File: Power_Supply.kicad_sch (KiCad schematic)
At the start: 23 parts, among them J1 Barrel_Jack, Q25 KSP2907A, Q26 IRF644, SW1 PB400EEQX, U1 L7805, U2 MC34063AP

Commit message: layout started
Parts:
- added C9: 100n, Capacitor_THT:C_Rect_L7.0mm_W2.5mm_P5.00mm, symbol Device:C
- F1: footprint Fuse:Fuseholder_Cylinder-5x20mm_Schurter_0031_8201_Horizontal_Open -> NixieClock:5x20 fuse
- Q25: footprint Package_TO_SOT_THT:TO-92_Inline -> Package_TO_SOT_THT:TO-92_Inline_Wide
- SW1: footprint Button_Switch_THT:SW_NKK_BB15AH -> NixieClock:PB400EEQX
- renumbered C9 to C10, C10 to C11, C11 to C12, C12 to C13, C13 to C14
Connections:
- net +12V: now also C9.1
- net GND: now also C9.2
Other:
- moved on the sheet: C10, C8, U1

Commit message: Layout completed
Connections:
- net SMPS_IN: now reaches L1.1, R51.1, R52.1, U2.1 (SwC), U2.7 (Ipk), U2.8 (DC)
- net SMPS_SW: now reaches D3.2 (A), L1.2, Q26.2 (D)
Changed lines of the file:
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@@
     (effects (font (size 2.0066 2.0066)) (justify left bottom))
+  )
+  (label "SMPS_OUT" (at 241.3 78.74 0)
+    (effects (font (size 1.27 1.27)) (justify left bottom))
+  )
+  (label "SMPS_SW" (at 223.52 77.47 180)
+    (effects (font (size 1.27 1.27)) (justify right bottom))
+  )
+  (label "SMPS_IN" (at 196.85 60.96 0)
+    (effects (font (size 1.27 1.27)) (justify left bottom))
   )
   (global_label "DISP_EN" (shape input) (at 128.27 45.72 180) (fields_autoplaced)

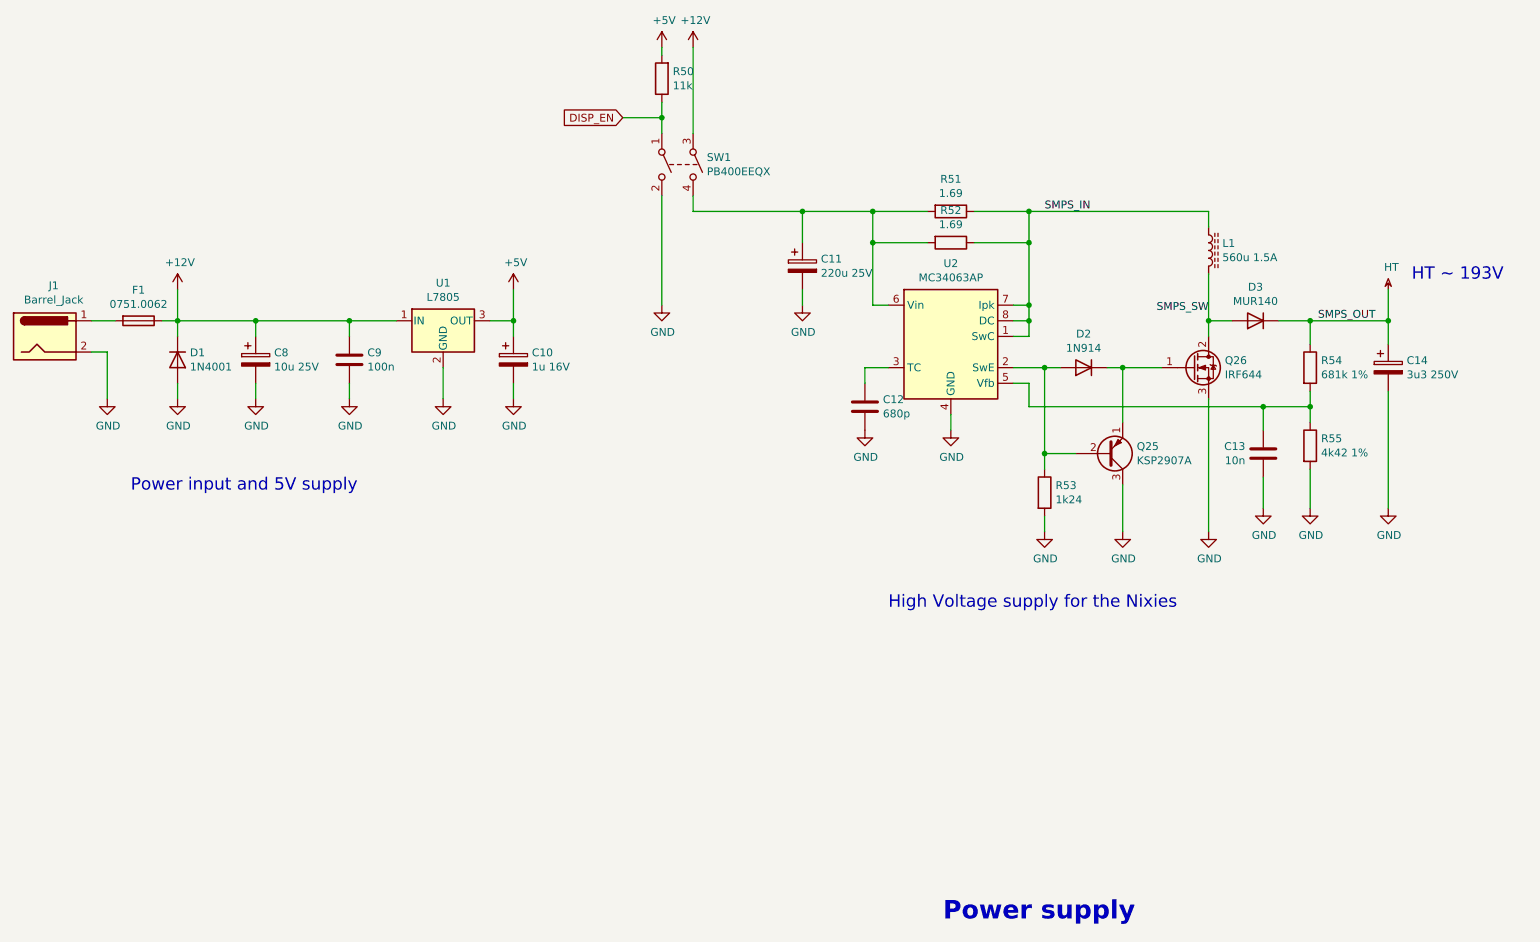
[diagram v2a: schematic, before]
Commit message: Pablo's review, several changes:
Schematic:
- Overall aesthetics
- Added PWR_FLAG to remove ERC errors.
Layout:
- Overall component alignment
- Removed some loops and unnecessary vias.
- Cleaned up vias without ends.
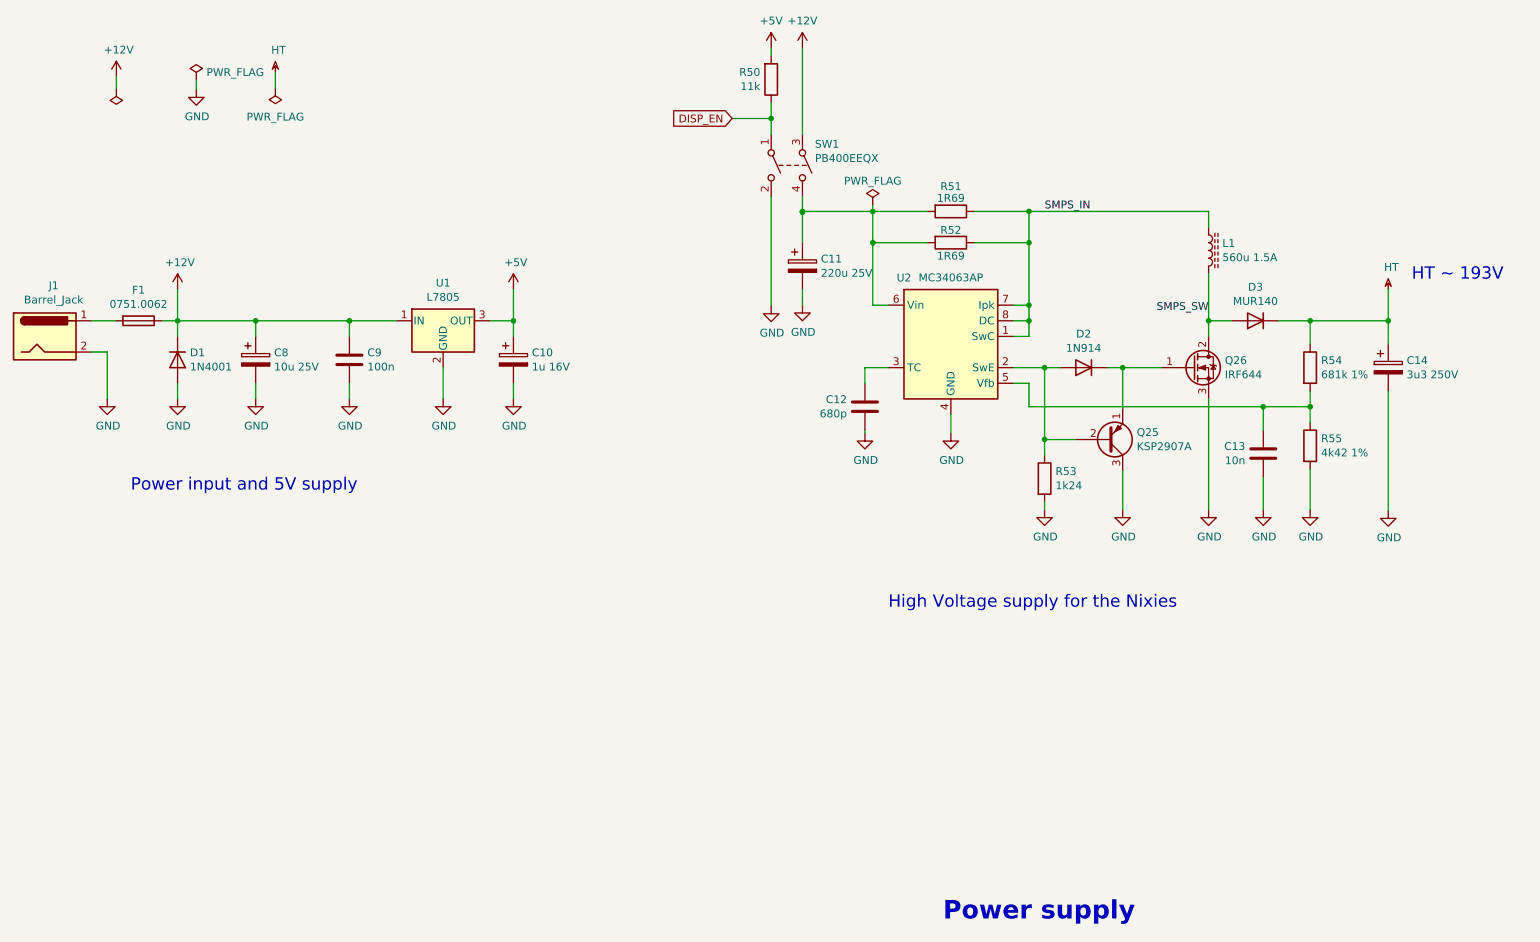
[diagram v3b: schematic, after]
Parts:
- R51, R52: value 1.69 -> 1R69
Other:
- moved on the sheet: Q25, R50, R53, SW1

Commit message: WIP
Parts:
- C13: footprint Capacitor_THT:C_Rect_L7.0mm_W2.5mm_P5.00mm -> Capacitor_SMD:C_0805_2012Metric
- R50, R51, R52, R53, R54, R55: footprint Resistor_THT:R_Axial_DIN0207_L6.3mm_D2.5mm_P10.16mm_Horizontal -> Resistor_SMD:R_0805_2012Metric
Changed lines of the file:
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@@
       (effects (font (size 1.27 1.27)) (justify left))
     )
-    (property "Footprint" "Resistor_THT:R_Axial_DIN0207_L6.3mm_D2.5mm_P10.16mm_Horizontal" (id 2) (at 195.072 104.394 90)
+    (property "Footprint" "Resistor_SMD:R_0805_2012Metric" (id 2) (at 195.072 104.394 90)
       (effects (font (size 1.27 1.27)) hide)
     )
@@
       (effects (font (size 1.27 1.27)) (justify left))
     )
-    (property "Footprint" "Capacitor_THT:C_Rect_L7.0mm_W2.5mm_P5.00mm" (id 2) (at 231.4448 104.14 0)
+    (property "Footprint" "Capacitor_SMD:C_0805_2012Metric" (id 2) (at 231.4448 104.14 0)
       (effects (font (size 1.27 1.27)) hide)
     )
@@
       (effects (font (size 1.27 1.27)) (justify left))
     )
-    (property "Footprint" "Resistor_THT:R_Axial_DIN0207_L6.3mm_D2.5mm_P10.16mm_Horizontal" (id 2) (at 238.252 86.36 90)
+    (property "Footprint" "Resistor_SMD:R_0805_2012Metric" (id 2) (at 238.252 86.36 90)
       (effects (font (size 1.27 1.27)) hide)
     )
@@
       (effects (font (size 1.27 1.27)) (justify left))
     )
-    (property "Footprint" "Resistor_THT:R_Axial_DIN0207_L6.3mm_D2.5mm_P10.16mm_Horizontal" (id 2) (at 238.252 99.06 90)
+    (property "Footprint" "Resistor_SMD:R_0805_2012Metric" (id 2) (at 238.252 99.06 90)
       (effects (font (size 1.27 1.27)) hide)
     )
@@
     (property "Reference" "R51" (id 0) (at 181.61 56.896 90))
     (property "Value" "1R69" (id 1) (at 181.61 58.801 90))
-    (property "Footprint" "Resistor_THT:R_Axial_DIN0207_L6.3mm_D2.5mm_P10.16mm_Horizontal" (id 2) (at 181.61 59.182 90)
+    (property "Footprint" "Resistor_SMD:R_0805_2012Metric" (id 2) (at 181.61 59.182 90)
       (effects (font (size 1.27 1.27)) hide)
     )
@@
     (property "Reference" "R52" (id 0) (at 181.61 64.008 90))
     (property "Value" "1R69" (id 1) (at 181.61 68.199 90))
-    (property "Footprint" "Resistor_THT:R_Axial_DIN0207_L6.3mm_D2.5mm_P10.16mm_Horizontal" (id 2) (at 181.61 64.262 90)
+    (property "Footprint" "Resistor_SMD:R_0805_2012Metric" (id 2) (at 181.61 64.262 90)
       (effects (font (size 1.27 1.27)) hide)
     )
@@
       (effects (font (size 1.27 1.27)) (justify right))
     )
-    (property "Footprint" "Resistor_THT:R_Axial_DIN0207_L6.3mm_D2.5mm_P10.16mm_Horizontal" (id 2) (at 150.622 39.497 90)
+    (property "Footprint" "Resistor_SMD:R_0805_2012Metric" (id 2) (at 150.622 39.497 90)
       (effects (font (size 1.27 1.27)) hide)
     )
@@
       (effects (font (size 1.27 1.27)) hide)
     )
-    (property "Value" "" (id 1) (at 45.9232 45.6946 0))
+    (property "Value" "PWR_FLAG" (id 1) (at 45.9232 45.6946 0))
     (property "Footprint" "" (id 2) (at 45.9232 40.9956 0)
       (effects (font (size 1.27 1.27)) hide)
